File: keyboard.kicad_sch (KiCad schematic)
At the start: 28 parts, among them J1 Conn_01x02, P1 USB_C_Plug_USB2.0, U1 RP2040, U2 NCP1117-3.3_SOT223, U3 W25Q128JVS, Y1 Crystal_GND24

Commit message: same as previous commit, just forgot to save
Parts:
- C15, C16: value C -> 15p
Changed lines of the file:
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@@
 			)
 		)
-		(property "Value" "C"
+		(property "Value" "15p"
 			(at 55.88 355.6 90)
 			(show_name no)
@@
 			)
 		)
-		(property "Value" "C"
+		(property "Value" "15p"
 			(at 55.88 332.74 90)
 			(show_name no)

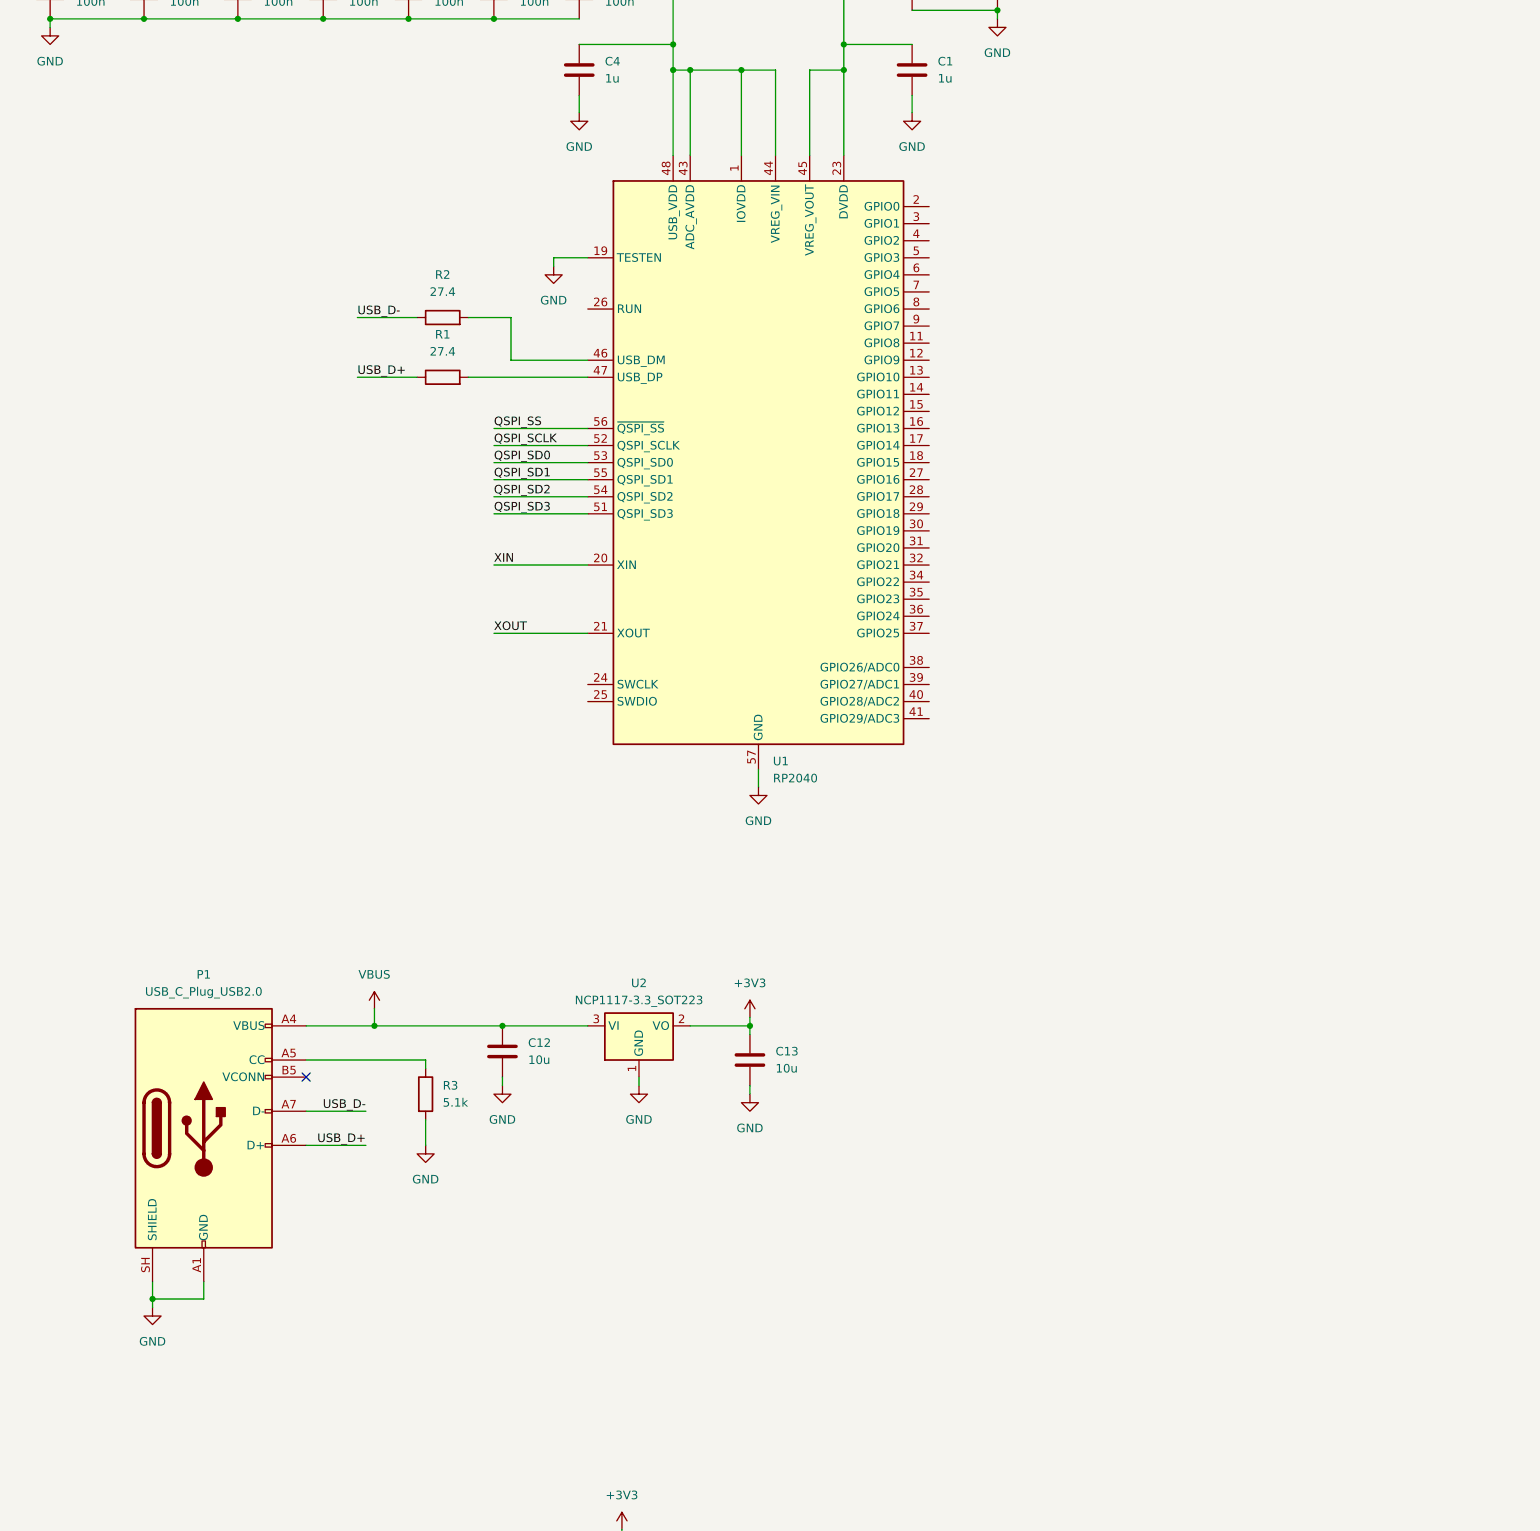
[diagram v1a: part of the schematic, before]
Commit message: modified schematic, may revert to original implementation
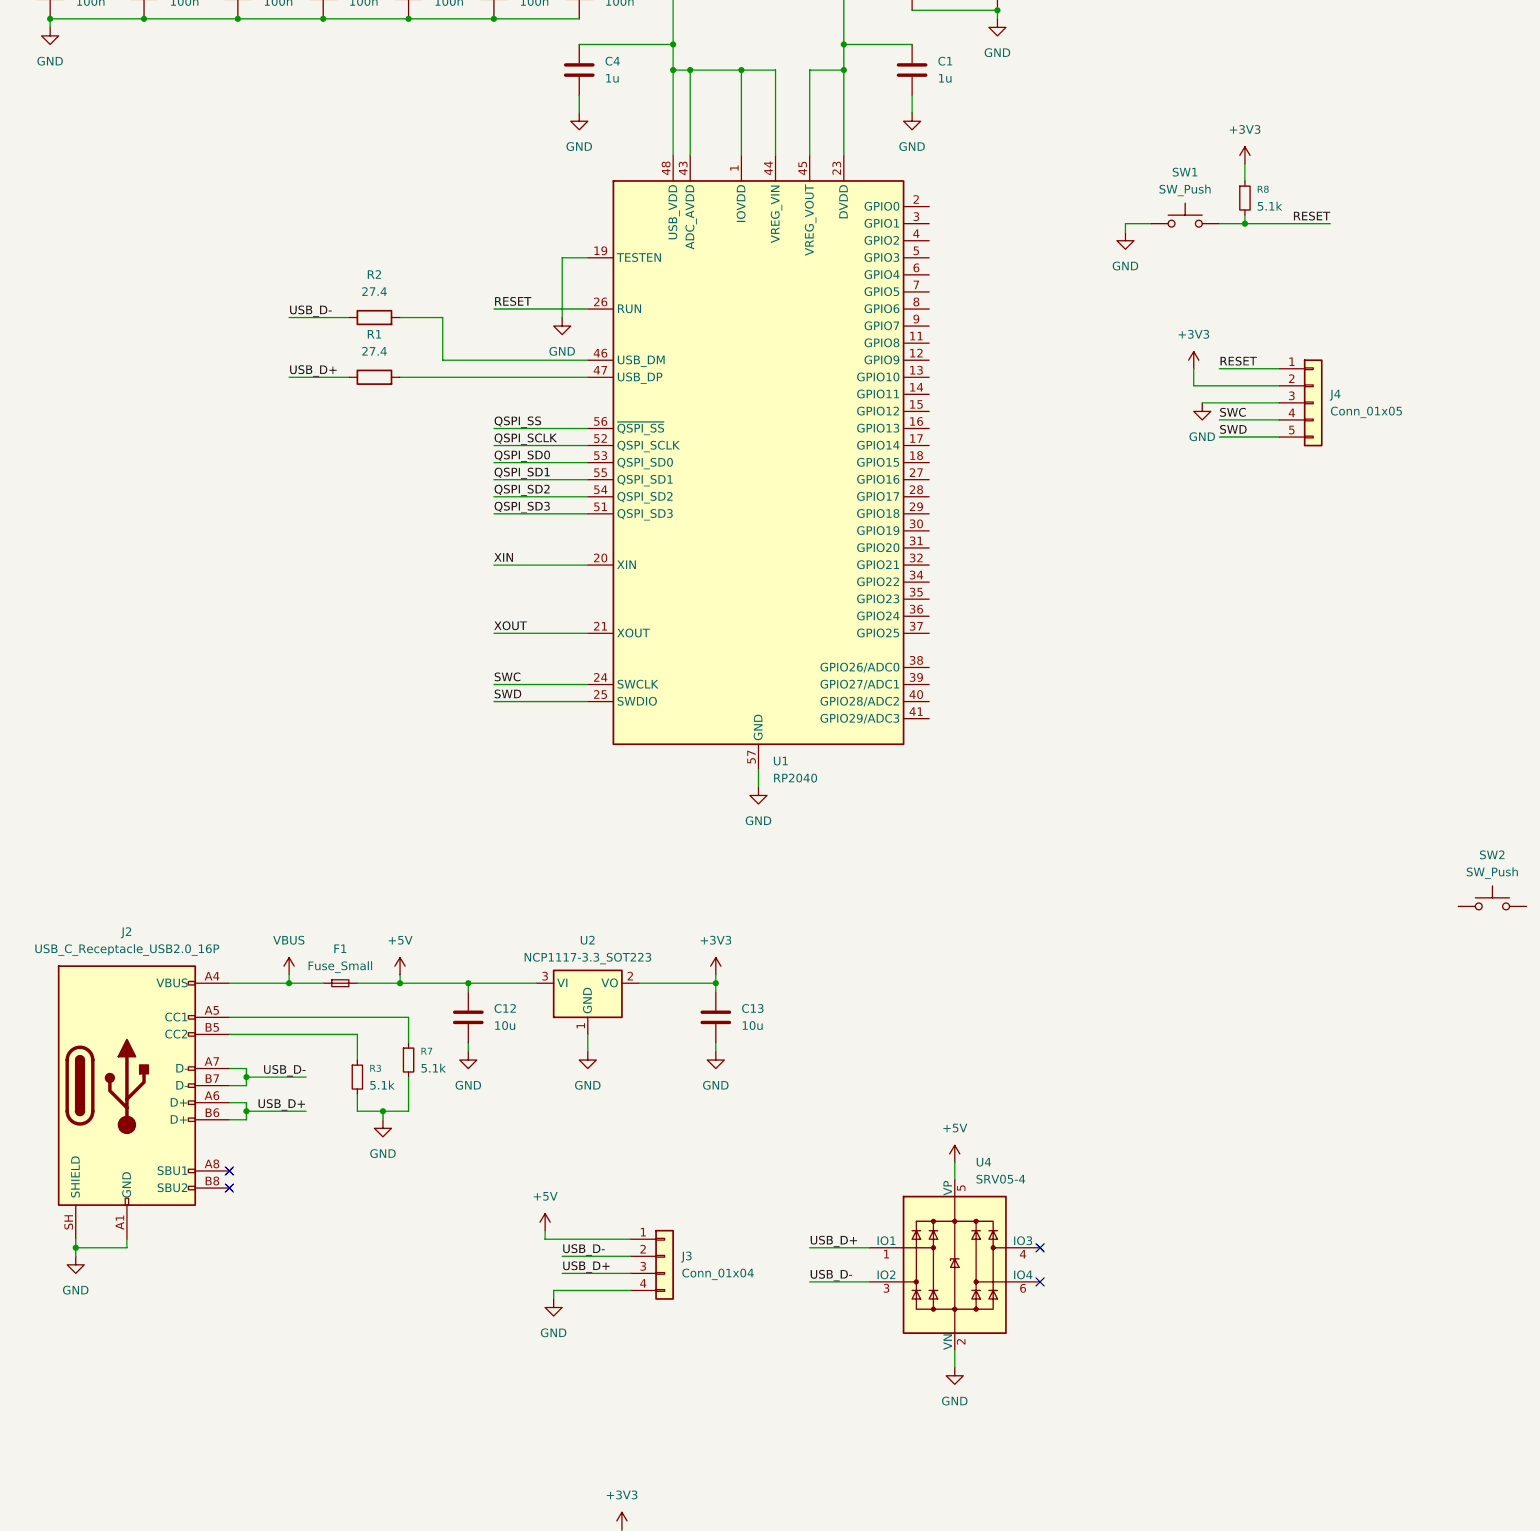
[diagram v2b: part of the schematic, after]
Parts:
- removed P1: USB_C_Plug_USB2.0, symbol Connector:USB_C_Plug_USB2.0
- removed R3: 5.1k, symbol Device:R
- added F1: Fuse_Small, symbol Device:Fuse_Small
- added J2: USB_C_Receptacle_USB2.0_16P, symbol Connector:USB_C_Receptacle_USB2.0_16P
- added J3: Conn_01x04, symbol Connector_Generic:Conn_01x04
- added J4: Conn_01x05, symbol Connector_Generic:Conn_01x05
- added R3, R7, R8: 5.1k, symbol Device:R_Small
- added SW1, SW2: SW_Push, symbol Switch:SW_Push
- added U4: SRV05-4, Package_TO_SOT_SMD:SOT-23-6, symbol Power_Protection:SRV05-4
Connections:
- net +3V3: now also J4.2 (Pin_2), R8.1
- net GND: now also J2.A1 (GND), J2.A12 (GND), J2.B1 (GND), J2.B12 (GND), J2.SH (SHIELD), J3.4 (Pin_4), J4.3 (Pin_3), R3.2, R7.2, SW1.1, U4.2 (VN)
- net USB_D+: now also J2.A6 (D+), J2.B6 (D+), J3.3 (Pin_3), U4.1 (IO1)
- net USB_D-: now also J2.A7 (D-), J2.B7 (D-), J3.2 (Pin_2), U4.3 (IO2)
- net VBUS: now also F1.1, J2.A4 (VBUS), J2.A9 (VBUS), J2.B4 (VBUS), J2.B9 (VBUS); no longer C12.1, U2.3 (VI)
- net SWC: now reaches U1.24 (SWCLK)
- net SWC: now also J4.4 (Pin_4)
- net SWD: now reaches U1.25 (SWDIO)
- net SWD: now also J4.5 (Pin_5)
- net RESET: now reaches U1.26 (RUN)
- net RESET: now also J4.1 (Pin_1), R8.2, SW1.2
- new net: J2.B5 (CC2), R3.1
- new net: J2.A5 (CC1), R7.1
- new net +5V: C12.1, F1.2, J3.1 (Pin_1), U2.3 (VI), U4.5 (VP)
- no-connect marks 1 -> 4
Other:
- moved on the sheet: C12, C13, R1, R2, U2

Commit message: Revert "same as previous commit, just forgot to save"
This reverts commit 4c8de7e3a9b6fdb7ebe3497e6038ce241e1c6b46.
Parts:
- C15, C16: value 15p -> C
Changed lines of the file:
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@@
 			)
 		)
-		(property "Value" "15p"
+		(property "Value" "C"
 			(at 55.88 355.6 90)
 			(show_name no)
@@
 			)
 		)
-		(property "Value" "15p"
+		(property "Value" "C"
 			(at 55.88 332.74 90)
 			(show_name no)

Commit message: add matrix to the schematic and corresponding netlists resolve ERC issues, probably PWR_FLAGS to pwr symbols
additionally need ot select footprints before PCB implementation
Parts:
- removed J1: Conn_01x02, symbol Connector_Generic:Conn_01x02
- removed R4: DNF, symbol Device:R
- removed R5: 1k, symbol Device:R
- added D1, D10, D11, D12, D13, D14, D15, D16, D17, D18, D19, D2, D20, D21, D22, D23, D24, D25, D26, D27, D28, D29, D3, D30, D31, D32, D33, D34, D35, D36, D37, D38, D39, D4, D40, D41, D42, D43, D44, D45, D46, D47, D48, D49, D5, D50, D51, D52, D53, D54, D55, D56, D57, D58, D59, D6, D60, D61, D62, D63, D64, D65, D66, D67, D68, D69, D7, D70, D71, D72, D73, D74, D75, D76, D77, D78, D79, D8, D80, D81, D82, D83, D84, D9: D_Small, symbol Device:D_Small
- added MX1, MX10, MX11, MX12, MX13, MX14, MX15, MX16, MX17, MX18, MX19, MX2, MX20, MX21, MX22, MX23, MX24, MX25, MX26, MX27, MX28, MX29, MX3, MX30, MX31, MX32, MX33, MX34, MX35, MX36, MX37, MX38, MX39, MX4, MX40, MX41, MX42, MX43, MX44, MX45, MX46, MX47, MX48, MX49, MX5, MX50, MX51, MX52, MX53, MX54, MX55, MX56, MX57, MX58, MX59, MX6, MX60, MX61, MX62, MX63, MX64, MX65, MX66, MX67, MX68, MX69, MX7, MX70, MX71, MX72, MX73, MX74, MX75, MX76, MX77, MX78, MX79, MX8, MX80, MX81, MX82, MX83, MX84, MX9: MX_SW_HS, PCM_marbastlib-mx:SW_MX_HS_CPG151101S11_1u, symbol PCM_marbastlib-mx:MX_SW_HS_CPG151101S11
- added R10, R11: 5.1k, symbol Device:R_Small
- added R9: 1k, symbol Device:R_Small
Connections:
- net +3V3: now also R11.2
- net GND: now also SW2.1
- net QSPI_SS: now also R10.1, R9.2
- net COL8: now reaches U1.11 (GPIO8)
- net COL8: now also MX23.1, MX37.1, MX51.1, MX65.1, MX79.1, MX9.1
- net COL9: now reaches U1.12 (GPIO9)
- net COL9: now also MX10.1, MX24.1, MX38.1, MX52.1, MX66.1, MX80.1
- net COL10: now reaches U1.13 (GPIO10)
- net COL10: now also MX11.1, MX25.1, MX39.1, MX53.1, MX67.1, MX81.1
- net COL11: now reaches U1.14 (GPIO11)
- net COL11: now also MX12.1, MX26.1, MX40.1, MX54.1, MX68.1, MX82.1
- net COL12: now reaches U1.15 (GPIO12)
- net COL12: now also MX13.1, MX27.1, MX41.1, MX55.1, MX69.1, MX83.1
- net COL13: now reaches U1.16 (GPIO13)
- net COL13: now also MX14.1, MX28.1, MX42.1, MX56.1, MX70.1, MX84.1
- net ROW0: now reaches U1.17 (GPIO14)
- net ROW0: now also D1.1 (K), D10.1 (K), D11.1 (K), D12.1 (K), D13.1 (K), D14.1 (K), D2.1 (K), D3.1 (K), D4.1 (K), D5.1 (K), D6.1 (K), D7.1 (K), D8.1 (K), D9.1 (K)
- net ROW1: now reaches U1.18 (GPIO15)
- net ROW1: now also D15.1 (K), D16.1 (K), D17.1 (K), D18.1 (K), D19.1 (K), D20.1 (K), D21.1 (K), D22.1 (K), D23.1 (K), D24.1 (K), D25.1 (K), D26.1 (K), D27.1 (K), D28.1 (K)
- net COL0: now reaches U1.2 (GPIO0)
- net COL0: now also MX1.1, MX15.1, MX29.1, MX43.1, MX57.1, MX71.1
- net ROW2: now reaches U1.27 (GPIO16)
- net ROW2: now also D29.1 (K), D30.1 (K), D31.1 (K), D32.1 (K), D33.1 (K), D34.1 (K), D35.1 (K), D36.1 (K), D37.1 (K), D38.1 (K), D39.1 (K), D40.1 (K), D41.1 (K), D42.1 (K)
- net ROW3: now reaches U1.28 (GPIO17)
- net ROW3: now also D43.1 (K), D44.1 (K), D45.1 (K), D46.1 (K), D47.1 (K), D48.1 (K), D49.1 (K), D50.1 (K), D51.1 (K), D52.1 (K), D53.1 (K), D54.1 (K), D55.1 (K), D56.1 (K)
- net ROW4: now reaches U1.29 (GPIO18)
- net ROW4: now also D57.1 (K), D58.1 (K), D59.1 (K), D60.1 (K), D61.1 (K), D62.1 (K), D63.1 (K), D64.1 (K), D65.1 (K), D66.1 (K), D67.1 (K), D68.1 (K), D69.1 (K), D70.1 (K)
- net COL1: now reaches U1.3 (GPIO1)
- net COL1: now also MX16.1, MX2.1, MX30.1, MX44.1, MX58.1, MX72.1
- net ROW5: now reaches U1.30 (GPIO19)
- net ROW5: now also D71.1 (K), D72.1 (K), D73.1 (K), D74.1 (K), D75.1 (K), D76.1 (K), D77.1 (K), D78.1 (K), D79.1 (K), D80.1 (K), D81.1 (K), D82.1 (K), D83.1 (K), D84.1 (K)
- net COL2: now reaches U1.4 (GPIO2)
- net COL2: now also MX17.1, MX3.1, MX31.1, MX45.1, MX59.1, MX73.1
- net COL3: now reaches U1.5 (GPIO3)
- net COL3: now also MX18.1, MX32.1, MX4.1, MX46.1, MX60.1, MX74.1
- net COL4: now reaches U1.6 (GPIO4)
- net COL4: now also MX19.1, MX33.1, MX47.1, MX5.1, MX61.1, MX75.1
- net COL5: now reaches U1.7 (GPIO5)
- net COL5: now also MX20.1, MX34.1, MX48.1, MX6.1, MX62.1, MX76.1
- net COL6: now reaches U1.8 (GPIO6)
- net COL6: now also MX21.1, MX35.1, MX49.1, MX63.1, MX7.1, MX77.1
- net COL7: now reaches U1.9 (GPIO7)
- net COL7: now also MX22.1, MX36.1, MX50.1, MX64.1, MX78.1, MX8.1
- net at SW2.2: now also R9.1
- new net: D81.2 (A), MX81.2
- new net: D70.2 (A), MX70.2
- new net: D9.2 (A), MX9.2
- new net: D80.2 (A), MX80.2
- new net: D71.2 (A), MX71.2
- new net: D21.2 (A), MX21.2
- new net: D63.2 (A), MX63.2
- new net: D56.2 (A), MX56.2
- new net: D83.2 (A), MX83.2
- new net: D65.2 (A), MX65.2
- new net: D55.2 (A), MX55.2
- new net: D72.2 (A), MX72.2
- new net: D40.2 (A), MX40.2
- new net: D49.2 (A), MX49.2
- new net: D12.2 (A), MX12.2
- new net: D52.2 (A), MX52.2
- new net: D27.2 (A), MX27.2
- new net: D74.2 (A), MX74.2
- new net: D29.2 (A), MX29.2
- new net: D24.2 (A), MX24.2
- new net: D42.2 (A), MX42.2
- new net: D76.2 (A), MX76.2
- new net: D26.2 (A), MX26.2
- new net: D45.2 (A), MX45.2
- new net: D35.2 (A), MX35.2
- new net: D37.2 (A), MX37.2
- new net: D84.2 (A), MX84.2
- new net: D4.2 (A), MX4.2
- new net: D13.2 (A), MX13.2
- new net: R10.2, R11.1
- new net: D32.2 (A), MX32.2
- new net: D8.2 (A), MX8.2
- new net: D19.2 (A), MX19.2
- new net: D69.2 (A), MX69.2
- new net: D73.2 (A), MX73.2
- new net: D58.2 (A), MX58.2
- new net: D62.2 (A), MX62.2
- new net: D15.2 (A), MX15.2
- new net: D6.2 (A), MX6.2
- new net: D34.2 (A), MX34.2
- new net: D59.2 (A), MX59.2
- new net: D82.2 (A), MX82.2
- new net: D3.2 (A), MX3.2
- new net: D14.2 (A), MX14.2
- new net: D18.2 (A), MX18.2
- new net: D66.2 (A), MX66.2
- new net: D38.2 (A), MX38.2
- new net: D51.2 (A), MX51.2
- new net: D36.2 (A), MX36.2
- new net: D28.2 (A), MX28.2
- new net: D30.2 (A), MX30.2
- new net: D61.2 (A), MX61.2
- new net: D2.2 (A), MX2.2
- new net: D7.2 (A), MX7.2
- new net: D11.2 (A), MX11.2
- new net: D31.2 (A), MX31.2
- new net: D79.2 (A), MX79.2
- new net: D64.2 (A), MX64.2
- new net: D5.2 (A), MX5.2
- new net: D53.2 (A), MX53.2
- new net: D1.2 (A), MX1.2
- new net: D75.2 (A), MX75.2
- new net: D47.2 (A), MX47.2
- new net: D41.2 (A), MX41.2
- new net: D25.2 (A), MX25.2
- new net: D10.2 (A), MX10.2
- new net: D44.2 (A), MX44.2
- new net: D46.2 (A), MX46.2
- new net: D67.2 (A), MX67.2
- new net: D23.2 (A), MX23.2
- new net: D33.2 (A), MX33.2
- new net: D48.2 (A), MX48.2
- new net: D77.2 (A), MX77.2
- new net: D22.2 (A), MX22.2
- new net: D43.2 (A), MX43.2
- new net: D17.2 (A), MX17.2
- new net: D16.2 (A), MX16.2
- new net: D54.2 (A), MX54.2
- new net: D60.2 (A), MX60.2
- new net: D57.2 (A), MX57.2
- new net: D78.2 (A), MX78.2
- new net: D68.2 (A), MX68.2
- new net: D39.2 (A), MX39.2
- new net: D50.2 (A), MX50.2
- new net: D20.2 (A), MX20.2
- no-connect marks 4 -> 15
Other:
- moved on the sheet: C12, C13, C14, C15, C16, F1, J2, J3, J4, R3, R6, R7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

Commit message: schematic satisfies ERC, begin footprint implementation
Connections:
- no-connect marks 15 -> 14

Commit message: update pcb
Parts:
- added S30: MX_stab, PCM_marbastlib-mx:STAB_MX_P_2u, symbol PCM_marbastlib-mx:MX_stab
- added S59, S61: MX_stab, PCM_marbastlib-mx:STAB_MX_P_2.25u, symbol PCM_marbastlib-mx:MX_stab
- added S78: MX_stab, PCM_marbastlib-mx:STAB_MX_P_6.25u, symbol PCM_marbastlib-mx:MX_stab
- C1, C10, C11, C14, C15, C16, C2, C3, C4, C5, C6, C7, C8, C9: footprint (none) -> Capacitor_SMD:C_0402_1005Metric
- C12, C13: footprint (none) -> Capacitor_SMD:C_0603_1608Metric
- D1, D10, D11, D12, D13, D14, D15, D16, D17, D18, D19, D2, D20, D21, D22, D23, D24, D25, D26, D27, D28, D29, D3, D30, D31, D32, D33, D34, D35, D36, D37, D38, D39, D4, D40, D41, D42, D43, D44, D45, D46, D47, D48, D49, D5, D50, D51, D52, D53, D54, D55, D56, D57, D58, D59, D6, D60, D61, D62, D63, D64, D65, D66, D67, D68, D69, D7, D70, D71, D72, D73, D74, D75, D76, D77, D78, D79, D8, D80, D81, D82, D83, D84, D9: footprint (none) -> Diode_SMD:D_SOD-123
- F1: footprint (none) -> Fuse:Fuse_1206_3216Metric
- J2: footprint (none) -> Connector_USB:USB_C_Receptacle_HRO_TYPE-C-31-M-12
- J3: footprint (none) -> Connector_JST:JST_SH_SM04B-SRSS-TB_1x04-1MP_P1.00mm_Horizontal
- J4: footprint (none) -> Connector_PinHeader_2.54mm:PinHeader_1x05_P2.54mm_Vertical
- MX32, MX45: footprint PCM_marbastlib-mx:SW_MX_HS_CPG151101S11_1u -> PCM_marbastlib-mx:SW_MX_HS_CPG151101S11_1.5u
- MX47, MX72: footprint PCM_marbastlib-mx:SW_MX_HS_CPG151101S11_1u -> PCM_marbastlib-mx:SW_MX_HS_CPG151101S11_1.75u
- MX75, MX76, MX77: footprint PCM_marbastlib-mx:SW_MX_HS_CPG151101S11_1u -> PCM_marbastlib-mx:SW_MX_HS_CPG151101S11_1.25u
- R1, R10, R11, R2, R3, R6, R7, R8, R9: footprint (none) -> Resistor_SMD:R_0402_1005Metric
- SW1, SW2: footprint (none) -> Button_Switch_SMD:SW_SPST_TL3342
- Y1: footprint (none) -> Crystal:Crystal_SMD_3225-4Pin_3.2x2.5mm
